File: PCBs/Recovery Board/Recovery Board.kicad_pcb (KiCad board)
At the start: 2 copper layers, 73.7 x 50.8 mm, 21 parts, among them U1 R-78E3.3-0.5, X1 XBee-S2C

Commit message: pinout changes
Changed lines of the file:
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@@
     (links 31)
     (no_connects 0)
-    (area 93.904999 98.984999 167.715001 149.935001)
+    (area 72.738857 82.136 204.493715 154.999)
     (thickness 1.6)
     (drawings 22)
@@
       (rotate (xyz 0 0 0))
     )
-  )
-  (module PayloadBoards:CPC1002NTR (layer F.Cu)
-    (at 132.08 132.08)
-    (fp_text reference S1 (at 0 -0.254) (layer F.SilkS) hide
-      (effects (font (size 1 1) (thickness 0.15)))
-    )
-    (fp_text value CPC1002N (at 2.032 -10.16) (layer F.Fab) hide
-      (effects (font (size 1 1) (thickness 0.15)))
-    )
-    (fp_line (start -2.0445 1.905) (end 2.0445 1.905) (layer F.SilkS) (width 0.15))
-    (fp_line (start -2.0445 -1.905) (end 2.0445 -1.905) (layer F.SilkS) (width 0.15))
-    (fp_line (start 2.0445 -1.905) (end 2.0445 1.905) (layer F.SilkS) (width 0.15))
-    (fp_line (start -2.0445 -1.905) (end -2.0445 1.905) (layer F.SilkS) (width 0.15))
-    (pad 2 smd oval (at 1.27 -2.8) (size 0.6 1.3) (layers F.Cu F.Paste F.Mask)
-      (net 3 GND))
-    (pad 1 smd oval (at -1.27 -2.8) (size 0.6 1.3) (layers F.Cu F.Paste F.Mask)
-      (net 34 "Net-(R1-Pad1)"))
-    (pad 4 smd oval (at 1.27 2.8) (size 0.6 1.3) (layers F.Cu F.Paste F.Mask)
-      (net 27 7.4V))
-    (pad 3 smd oval (at -1.27 2.8) (size 0.6 1.3) (layers F.Cu F.Paste F.Mask)
-      (net 31 GoPro_Power))
-  )
-  (module PayloadBoards:CPC1002NTR (layer F.Cu)
-    (at 125.73 132.08)
-    (fp_text reference S2 (at -0.254 0.254) (layer F.SilkS) hide
-      (effects (font (size 1 1) (thickness 0.15)))
-    )
-    (fp_text value CPC1002N (at -0.254 -10.16) (layer F.Fab) hide
-      (effects (font (size 1 1) (thickness 0.15)))
-    )
-    (fp_line (start -2.0445 1.905) (end 2.0445 1.905) (layer F.SilkS) (width 0.15))
-    (fp_line (start -2.0445 -1.905) (end 2.0445 -1.905) (layer F.SilkS) (width 0.15))
-    (fp_line (start 2.0445 -1.905) (end 2.0445 1.905) (layer F.SilkS) (width 0.15))
-    (fp_line (start -2.0445 -1.905) (end -2.0445 1.905) (layer F.SilkS) (width 0.15))
-    (pad 2 smd oval (at 1.27 -2.8) (size 0.6 1.3) (layers F.Cu F.Paste F.Mask)
-      (net 3 GND))
-    (pad 1 smd oval (at -1.27 -2.8) (size 0.6 1.3) (layers F.Cu F.Paste F.Mask)
-      (net 35 "Net-(R2-Pad1)"))
-    (pad 4 smd oval (at 1.27 2.8) (size 0.6 1.3) (layers F.Cu F.Paste F.Mask)
-      (net 33 Stratologger_Switch-))
-    (pad 3 smd oval (at -1.27 2.8) (size 0.6 1.3) (layers F.Cu F.Paste F.Mask)
-      (net 32 Stratologger_Switch+))
   )
   (module Mounting_Holes:MountingHole_3.2mm_M3 (layer F.Cu)
@@
       (xy -0.001755 -2.811832) (xy 0.000023 -2.81432) (xy 0.002958 -2.809977)) (layer F.SilkS) (width 0.01))
   )
+  (module PayloadBoards:CPC1002NTR (layer F.Cu)
+    (at 132.08 132.08)
+    (fp_text reference S1 (at -0.254 0.254) (layer F.SilkS) hide
+      (effects (font (size 1 1) (thickness 0.15)))
+    )
+    (fp_text value CPC1002N (at -0.254 -10.16) (layer F.Fab) hide
+      (effects (font (size 1 1) (thickness 0.15)))
+    )
+    (fp_line (start -2.0445 1.905) (end 2.0445 1.905) (layer F.SilkS) (width 0.15))
+    (fp_line (start -2.0445 -1.905) (end 2.0445 -1.905) (layer F.SilkS) (width 0.15))
+    (fp_line (start 2.0445 -1.905) (end 2.0445 1.905) (layer F.SilkS) (width 0.15))
+    (fp_line (start -2.0445 -1.905) (end -2.0445 1.905) (layer F.SilkS) (width 0.15))
+    (pad 2 smd oval (at 1.27 -2.8) (size 0.8 1.6) (layers F.Cu F.Paste F.Mask)
+      (net 3 GND))
+    (pad 1 smd oval (at -1.27 -2.8) (size 0.8 1.6) (layers F.Cu F.Paste F.Mask)
+      (net 34 "Net-(R1-Pad1)"))
+    (pad 4 smd oval (at 1.27 2.8) (size 0.8 1.6) (layers F.Cu F.Paste F.Mask)
+      (net 27 7.4V))
+    (pad 3 smd oval (at -1.27 2.8) (size 0.8 1.6) (layers F.Cu F.Paste F.Mask)
+      (net 31 GoPro_Power))
+  )
+  (module PayloadBoards:CPC1002NTR (layer F.Cu)
+    (at 125.73 132.08)
+    (fp_text reference S2 (at -0.254 0.254) (layer F.SilkS) hide
+      (effects (font (size 1 1) (thickness 0.15)))
+    )
+    (fp_text value CPC1002N (at -0.254 -10.16) (layer F.Fab) hide
+      (effects (font (size 1 1) (thickness 0.15)))
+    )
+    (fp_line (start -2.0445 1.905) (end 2.0445 1.905) (layer F.SilkS) (width 0.15))
+    (fp_line (start -2.0445 -1.905) (end 2.0445 -1.905) (layer F.SilkS) (width 0.15))
+    (fp_line (start 2.0445 -1.905) (end 2.0445 1.905) (layer F.SilkS) (width 0.15))
+    (fp_line (start -2.0445 -1.905) (end -2.0445 1.905) (layer F.SilkS) (width 0.15))
+    (pad 2 smd oval (at 1.27 -2.8) (size 0.8 1.6) (layers F.Cu F.Paste F.Mask)
+      (net 3 GND))
+    (pad 1 smd oval (at -1.27 -2.8) (size 0.8 1.6) (layers F.Cu F.Paste F.Mask)
+      (net 35 "Net-(R2-Pad1)"))
+    (pad 4 smd oval (at 1.27 2.8) (size 0.8 1.6) (layers F.Cu F.Paste F.Mask)
+      (net 33 Stratologger_Switch-))
+    (pad 3 smd oval (at -1.27 2.8) (size 0.8 1.6) (layers F.Cu F.Paste F.Mask)
+      (net 32 Stratologger_Switch+))
+  )
   (dimension 43.18 (width 0.3) (layer F.SilkS)
     (gr_text "43.180 mm" (at 176.356 124.46 90) (layer F.SilkS)
@@
   (segment (start 128.27 116.84) (end 121.92 116.84) (width 0.25) (layer F.Cu) (net 2))
   (segment (start 128.27 116.84) (end 128.27 116.84) (width 0.25) (layer F.Cu) (net 2))
-  (segment (start 125.71 114.3) (end 128.016 114.3) (width 0.25) (layer F.Cu) (net 3) (status 400000))
+  (segment (start 125.71 114.3) (end 128.016 114.3) (width 0.25) (layer F.Cu) (net 3))
   (via (at 128.016 114.3) (size 0.6) (drill 0.4) (layers F.Cu B.Cu) (net 3))
-  (segment (start 133.33 114.3) (end 135.636 114.3) (width 0.25) (layer F.Cu) (net 3) (status 400000))
+  (segment (start 133.33 114.3) (end 135.636 114.3) (width 0.25) (layer F.Cu) (net 3))
   (via (at 135.636 114.3) (size 0.6) (drill 0.4) (layers F.Cu B.Cu) (net 3))
-  (segment (start 123.11 119.38) (end 123.11 120.316) (width 0.25) (layer F.Cu) (net 3) (status 400000))
+  (segment (start 123.11 119.38) (end 123.11 120.316) (width 0.25) (layer F.Cu) (net 3))
   (via (at 123.952 121.158) (size 0.6) (drill 0.4) (layers F.Cu B.Cu) (net 3))
   (segment (start 123.11 120.316) (end 123.952 121.158) (width 0.25) (layer F.Cu) (net 3))

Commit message: stashing changes
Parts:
- added 2k1: R3, Resistors_SMD:R_0805_HandSoldering, F.Cu at (140.0, 161.3)
- added 3k1: R4, Resistors_SMD:R_0805_HandSoldering, F.Cu at (113.3, 156.5)
- added C3: 1uF, Capacitors_SMD:C_0805_HandSoldering, F.Cu at (137.7, 124.0)
- added C4: 8.2pF, Capacitors_SMD:C_0805_HandSoldering, F.Cu at (138.2, 118.9)
- moved X1 2.54 mm to (153.4, 131.6)
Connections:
- A1 pad 23: INSTRUMENT_ARDUINO_COMMS1 -> SDA
- A1 pad 24: INSTRUMENT_ARDUINO_COMMS2 -> SCL
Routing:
- net INSTRUMENT_ARDUINO_COMMS2: track 52.4 -> 47.7 mm
- net SCL: track 0.00 -> 4.67 mm
- net XBEE-DOUT: track 46.7 -> 49.2 mm
- net Net-(2k1-Pad1): track 17.5 -> 20.1 mm
- net Net-(C2-Pad1): track 15.1 -> 17.2 mm
- net SDA: track 0.00 -> 1.27 mm
- net INSTRUMENT_ARDUINO_COMMS1: track 45.3 -> 44.0 mm

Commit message: Updated Recovery Netlist, started board updated layout
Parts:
- removed 2k1: R3, Resistors_SMD:R_0805_HandSoldering
- removed 3k1: R4, Resistors_SMD:R_0805_HandSoldering
- added R5: 1.2k, Resistors_SMD:R_0805_HandSoldering, F.Cu at (118.4, 166.6)
- added R6: 1.2k, Resistors_SMD:R_0805_HandSoldering, F.Cu at (125.7, 177.0)
- added R7: 2k, Resistors_SMD:R_0805_HandSoldering, F.Cu at (131.6, 173.0)
- added R8: 3k, Resistors_SMD:R_0805_HandSoldering, F.Cu at (114.0, 161.5)
- added Strat: Conn_01x02, Connectors_Molex:Molex_KK-6410-02_02x2.54mm_Straight, F.Cu at (116.6, 143.5)
- added U2: PI4ULS5V201TAEX, sot:SOT-23-6, F.Cu at (135.9, 170.7)
- added U3: PI4ULS5V201TAEX, sot:SOT-23-6, F.Cu at (106.4, 173.5)
- R1, R2: value 1.9k -> 0
- R3: value R3 -> 0
- R4: value R4 -> 0
- moved A1 10.7 mm to (93.5, 104.1)
- moved REF** 10.7 mm to (87.1, 102.9)
- moved REF** 10.7 mm to (87.1, 146.1)
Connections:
- net Net-(C2-Pad1) renamed 3.3V
- A1 pad 1: XBEE-DOUT -> Net-(A1-Pad1)
- A1 pad 11: Net-(A1-Pad11) -> /Sheet5ABE85A8_2/A
- A1 pad 15: Net-(A1-Pad15) -> Stratologger_Relay
- A1 pad 16: Net-(A1-Pad16) -> Instr_Arduino_Relay
- A1 pad 2: XBEE-DIN -> Net-(A1-Pad2)
- R1 pad 1: Net-(R1-Pad1) -> Net-(A1-Pad1)
- R1 pad 2: Net-(A1-Pad16) -> XBEE-DIN
- R2 pad 1: Net-(R2-Pad1) -> Net-(A1-Pad2)
- R2 pad 2: Net-(A1-Pad16) -> /Sheet5ABE85A8/A
- R3 pad 1: Net-(2k1-Pad1) -> Net-(A1-Pad5)
- R3 pad 2: XBEE-DIN -> /Sheet5ABE85A8/A
- R4 pad 1: GND -> Net-(A1-Pad6)
- R4 pad 2: Net-(2k1-Pad1) -> XBEE-DIN
- S1 pad 1: Net-(R1-Pad1) -> Net-(R5-Pad1)
- S2 pad 1: Net-(R2-Pad1) -> Net-(R6-Pad1)
- X1 pad 3: Net-(2k1-Pad1) -> Net-(R7-Pad1)
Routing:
- net /Sheet5ABE85A8/A: track 0.00 -> 46.7 mm
- net XBEE-DIN: track 44.7 -> 7.77 mm
- net Net-(A1-Pad1): track 0.00 -> 34.8 mm
- net XBEE-DOUT: track 49.2 -> 17.9 mm
- net Net-(A1-Pad16): track 26.5 -> 0.00 mm
- net Net-(A1-Pad2): track 0.00 -> 24.3 mm
- net Net-(2k1-Pad1): track 20.1 -> 0.00 mm
- net Net-(A1-Pad5): track 0.00 -> 7.12 mm
- net Net-(R7-Pad1): track 0.00 -> 5.18 mm
- net GND: track 10.3 -> 14.3 mm, vias 5 -> 4
- net Instr_Arduino_Relay: track 0.00 -> 3.59 mm
- net Net-(R2-Pad1): track 3.47 -> 0.00 mm
- net Net-(R1-Pad1): track 3.47 -> 0.00 mm
- net Net-(A1-Pad6): track 0.00 -> 2.13 mm, vias 0 -> 1
- net INSTRUMENT_ARDUINO_COMMS1: track 44.0 -> 42.2 mm
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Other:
- board size 73.7 x 50.8 mm -> 84.3 x 50.8 mm

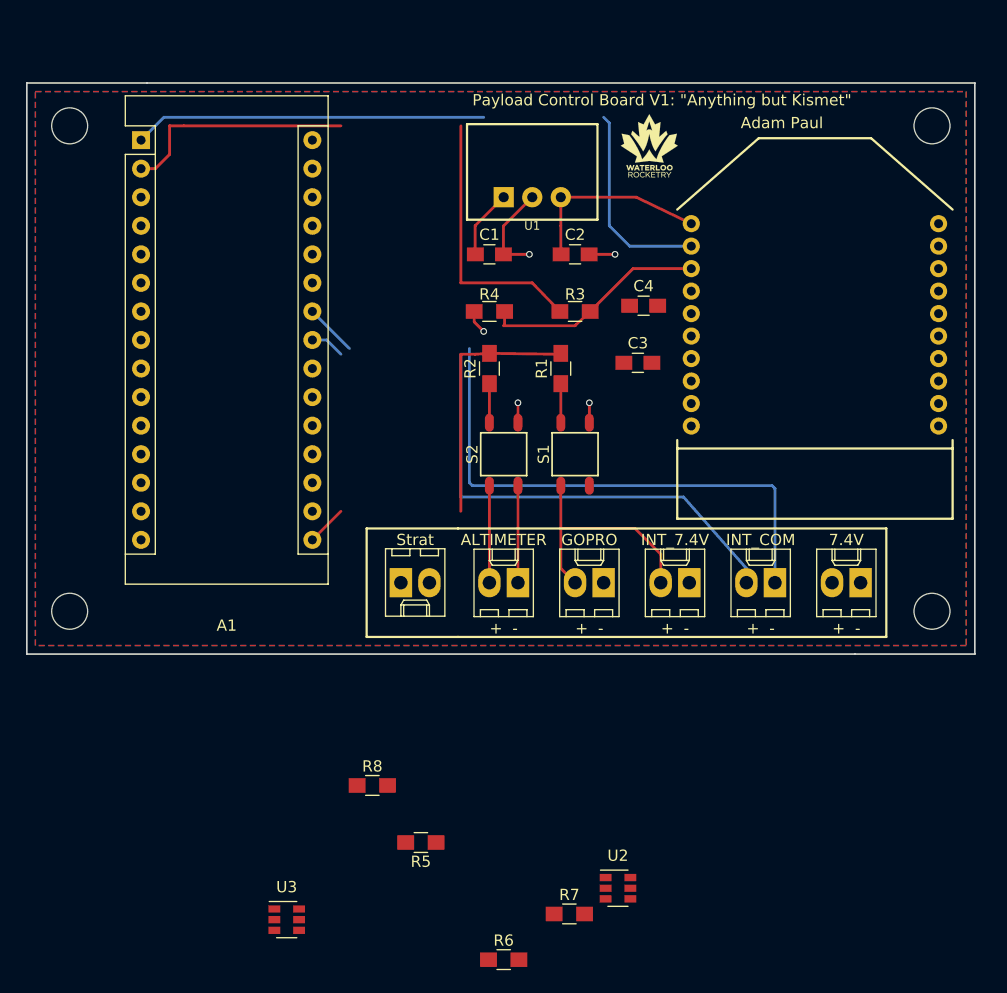
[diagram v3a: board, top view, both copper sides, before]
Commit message: Continued new recovery board layout
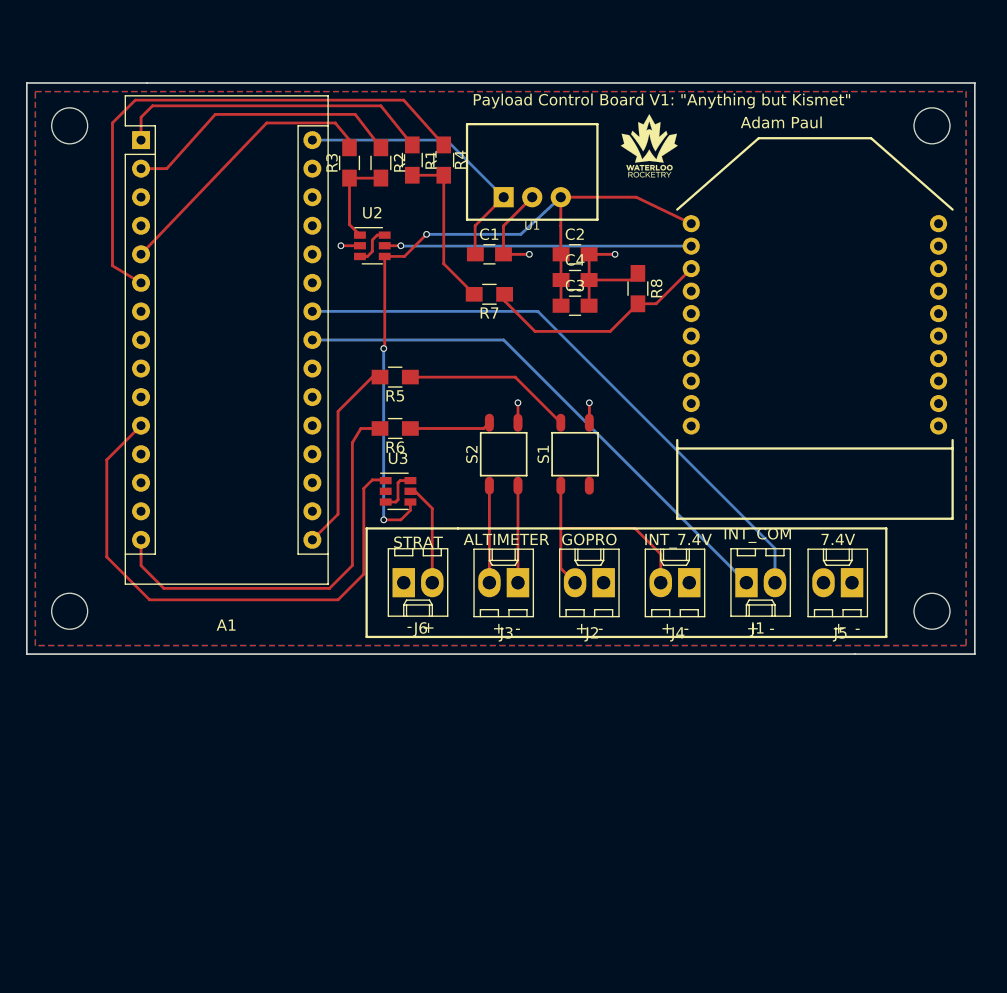
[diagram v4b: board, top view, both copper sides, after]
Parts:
- removed 7.4V, ALTIMETER, GOPRO, INT_7.4V, INT_COM, Strat: Conn_01x02, Connectors_Molex:Molex_KK-6410-02_02x2.54mm_Straight
- added J1: Conn_01x02, Connectors_Molex:Molex_KK-6410-02_02x2.54mm_Straight, F.Cu at (147.3, 143.5)
- added J2: Conn_01x02, Connectors_Molex:Molex_KK-6410-02_02x2.54mm_Straight, F.Cu at (134.6, 143.5)
- added J3: Conn_01x02, Connectors_Molex:Molex_KK-6410-02_02x2.54mm_Straight, F.Cu at (127.0, 143.5)
- added J4: Conn_01x02, Connectors_Molex:Molex_KK-6410-02_02x2.54mm_Straight, F.Cu at (142.2, 143.5)
- added J5: Conn_01x02, Connectors_Molex:Molex_KK-6410-02_02x2.54mm_Straight, F.Cu at (156.7, 143.5)
- added J6: Conn_01x02, Connectors_Molex:Molex_KK-6410-02_02x2.54mm_Straight, F.Cu at (116.8, 143.5)
- moved U2 61.2 mm to (114.0, 113.5)
- moved R7 55.6 mm to (124.5, 117.9), turned to 180 degrees
- moved R8 50.1 mm to (137.7, 117.3), turned to 270 degrees
- moved R6 48.2 mm to (116.1, 129.8), turned to 180 degrees
- moved R5 41.5 mm to (116.1, 125.2)
- moved U3 39.4 mm to (116.3, 135.4)
- moved R3 24.0 mm to (112.0, 106.2), turned to 270 degrees
- moved R1 22.8 mm to (117.6, 105.9), turned to 270 degrees
- moved R2 20.7 mm to (114.8, 106.2), turned to 270 degrees
- moved R4 14.1 mm to (120.4, 105.9), turned to 270 degrees
- moved C3 7.55 mm to (132.1, 118.9)
- moved C4 6.51 mm to (132.1, 116.6)
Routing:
- net 3.3V: track 17.2 -> 66.5 mm, vias 0 -> 3
- net /Sheet5ABE85A8_2/A: track 0.00 -> 48.3 mm
- net SCL: track 4.67 -> 52.9 mm
- net INSTRUMENT_ARDUINO_COMMS2: track 47.7 -> 0.00 mm
- net Net-(A1-Pad6): track 2.13 -> 47.8 mm, vias 1 -> 0
- net SDA: track 3.07 -> 47.6 mm
- net INSTRUMENT_ARDUINO_COMMS1: track 42.2 -> 0.00 mm
- net /Sheet5ABE85A8/A: track 46.7 -> 8.61 mm
- net Stratologger_Relay: track 0.00 -> 36.9 mm
- net 7.4V: track 6.13 -> 25.3 mm
- net Net-(A1-Pad5): track 7.12 -> 24.9 mm
- net Net-(R7-Pad1): track 5.18 -> 20.6 mm
- net Net-(R5-Pad1): track 0.00 -> 15.1 mm
- net Instr_Arduino_Relay: track 3.59 -> 17.4 mm
- net GND: track 14.3 -> 25.1 mm, vias 4 -> 5
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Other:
- board text added: "7.4V"
- board text added: "ALTIMETER"
- board text added: "GOPRO"
- board text added: "INT_7.4V"
- board text added: "INT_COM"
- board text added: "STRAT"

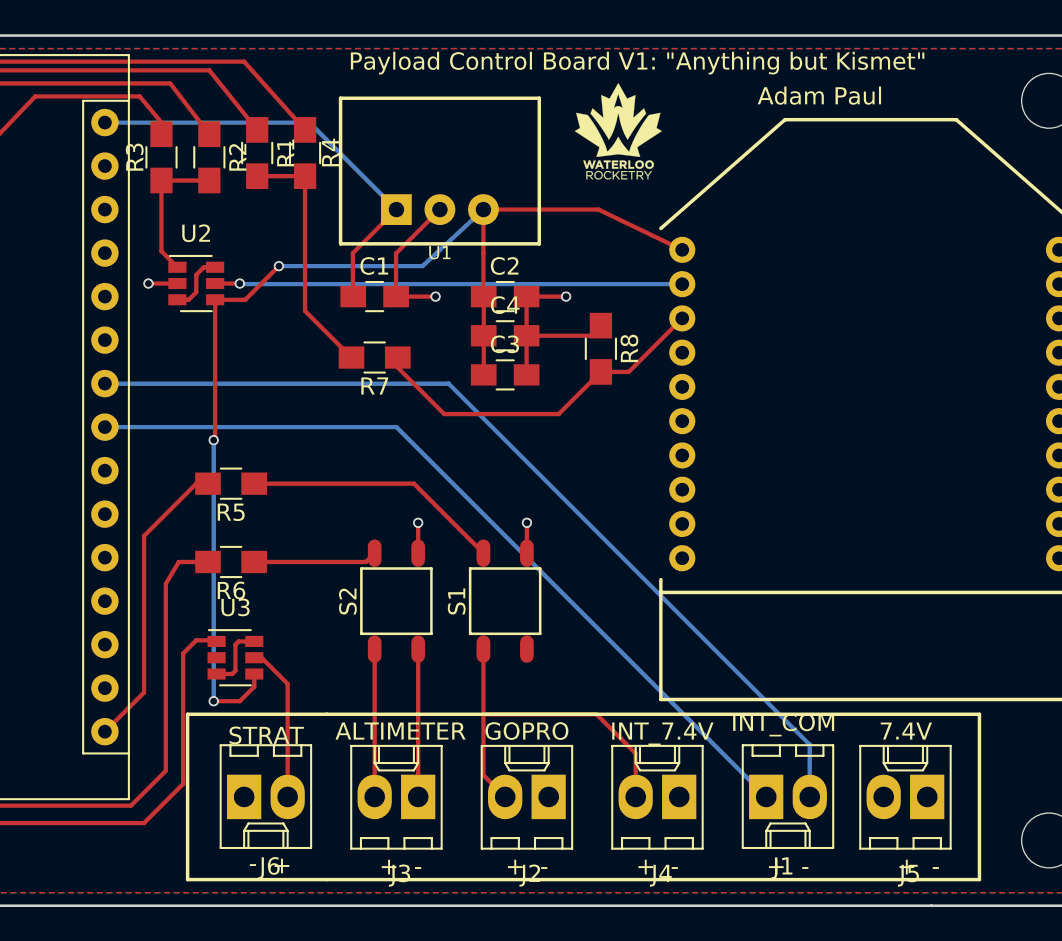
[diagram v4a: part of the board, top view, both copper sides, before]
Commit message: Finished updating recovery board layout
board layout, schematic and netlist up to date
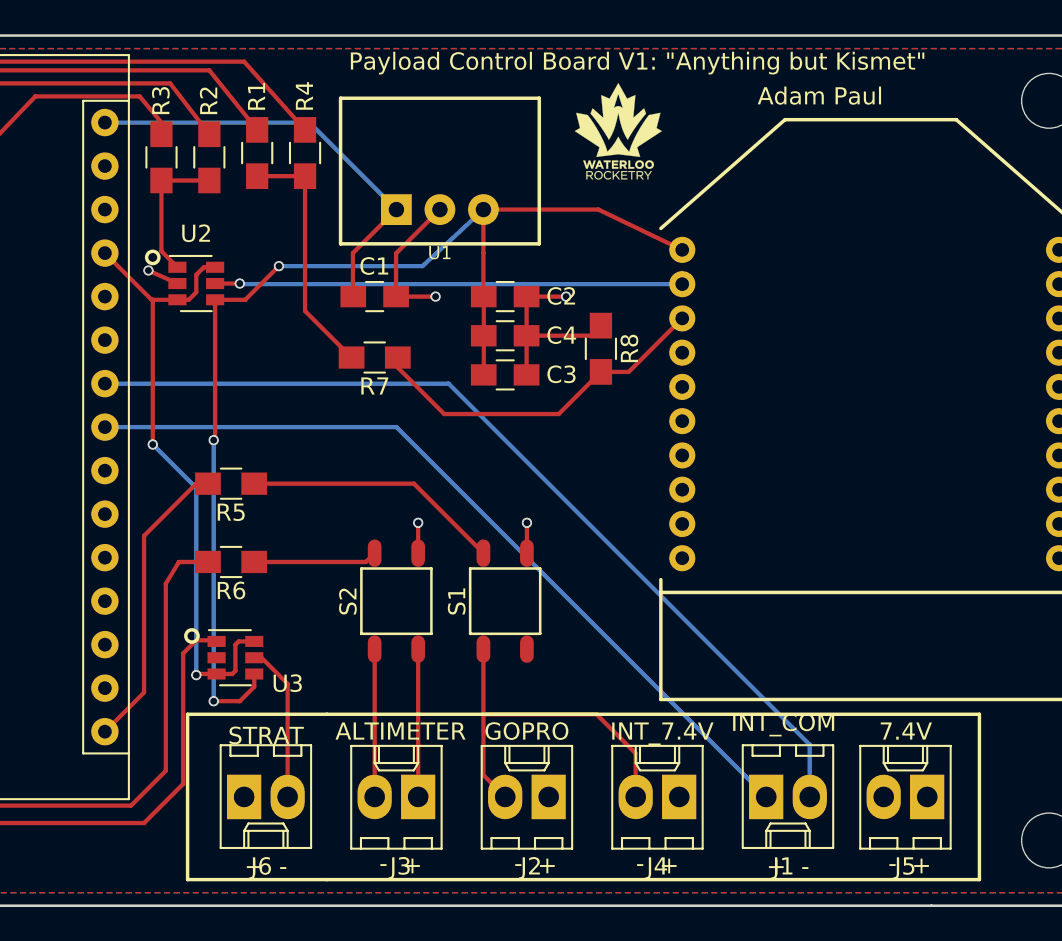
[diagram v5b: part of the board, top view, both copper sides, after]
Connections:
- A1 pad 27: Net-(A1-Pad27) -> 5V
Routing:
- net 5V: track 7.46 -> 37.0 mm, vias 0 -> 2
